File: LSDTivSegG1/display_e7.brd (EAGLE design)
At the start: 150 x 100 mm, 95 parts, among them IC1 MEGA8-P, IC2 MAX232, IC3 PCF8574P, IC4 PCF8574P, IC5 PCF8574P, IC6 PCF8574P

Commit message: exported the current version of the eagle 7 compatible file for display board
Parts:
- removed R4: 1k0, rcl:0207/10
- added C10, C11, C12, C13: 100nF, rcl:C025-025X050
- added JP2: (no value), pinhead:2X03
- R2: value 10k -> 5k
- R3: value 2k2 -> 15k
- U$2: value PCB -> DISPLAY_FRAME; device lsd2016:BOARD -> lsd2016:DISPLAY_FRAME
- moved LED19 255.4 mm to (127.0, 66.0), turned to 90 degrees
- moved R32 253.5 mm to (101.6, 38.1), turned to 270 degrees
- moved C7 246.0 mm to (121.9, 83.8), turned to 270 degrees
- moved IC6 245.8 mm to (137.2, 16.5), flipped to the bottom, turned to 180 degrees
- moved R31 242.0 mm to (99.1, 38.1), turned to 270 degrees
- moved LED18 234.9 mm to (119.4, 68.6), turned to 90 degrees
- moved R30 230.6 mm to (96.5, 38.1), turned to 270 degrees
- moved C5 229.5 mm to (121.9, 78.1), turned to 90 degrees
- moved IC2 229.5 mm to (108.6, 81.9)
- moved R5 227.3 mm to (82.5, 24.1)
- moved LED24 222.3 mm to (129.5, 27.9)
- moved U$1 221.2 mm to (113.0, 5.08), turned to 180 degrees
- moved JP1 220.3 mm to (73.7, 73.7), turned to 90 degrees
- moved R29 219.3 mm to (94.0, 38.1), turned to 270 degrees
- moved LED17 214.9 mm to (111.8, 68.6), turned to 90 degrees
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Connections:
- removed net VCC: IC2.16
- new net RS232RX_CON: JP2.3, X1.2
- new net RS232TX_CON: JP2.4, X1.3
- net +5V: now also C10.1, C11.1, C12.1, C13.1, IC2.16; no longer C6.-, R12.2, R13.2, R14.2, R15.2, R16.2, R17.2, R18.2, R19.2, R20.2, R21.2, R22.2, R23.2, R24.2, R25.2, R26.2, R27.2, R28.2, R29.2, R30.2, R31.2, R32.2, R33.2, R34.2, R35.2
- net GND: now also C10.2, C11.2, C12.2, C13.2, C6.-, R12.2, R13.2, R14.2, R15.2, R16.2, R17.2, R18.2, R19.2, R20.2, R21.2, R22.2, R23.2, R24.2, R25.2, R26.2, R27.2, R28.2, R29.2, R30.2, R31.2, R32.2, R33.2, R34.2, R35.2; no longer R4.2
- net N$9: no longer R4.1
- net RS232RX: now also JP2.1, JP2.6; no longer X1.4
- net RS232TX: now also JP2.2, JP2.5; no longer X1.3
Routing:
- net +5V: track 0.00 -> 159.8 mm
- net RW: track 0.00 -> 82.1 mm, vias 0 -> 1
- net RESET: track 0.00 -> 71.2 mm
- net RS232TX: track 0.00 -> 50.5 mm
- net N$34: track 0.00 -> 39.4 mm
- net N$22: track 0.00 -> 39.4 mm
- net RS232RX: track 0.00 -> 39.1 mm
- net N$35: track 0.00 -> 36.9 mm
- net N$23: track 0.00 -> 36.9 mm
- net N$21: track 0.00 -> 35.4 mm
- net N$33: track 0.00 -> 35.4 mm
- net N$32: track 0.00 -> 32.5 mm
- net N$20: track 0.00 -> 32.5 mm
- net N$19: track 0.00 -> 30.4 mm
- net N$31: track 0.00 -> 30.4 mm
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- added copper zone on layer 16, net GND
- removed copper zone on layer 1, net GND

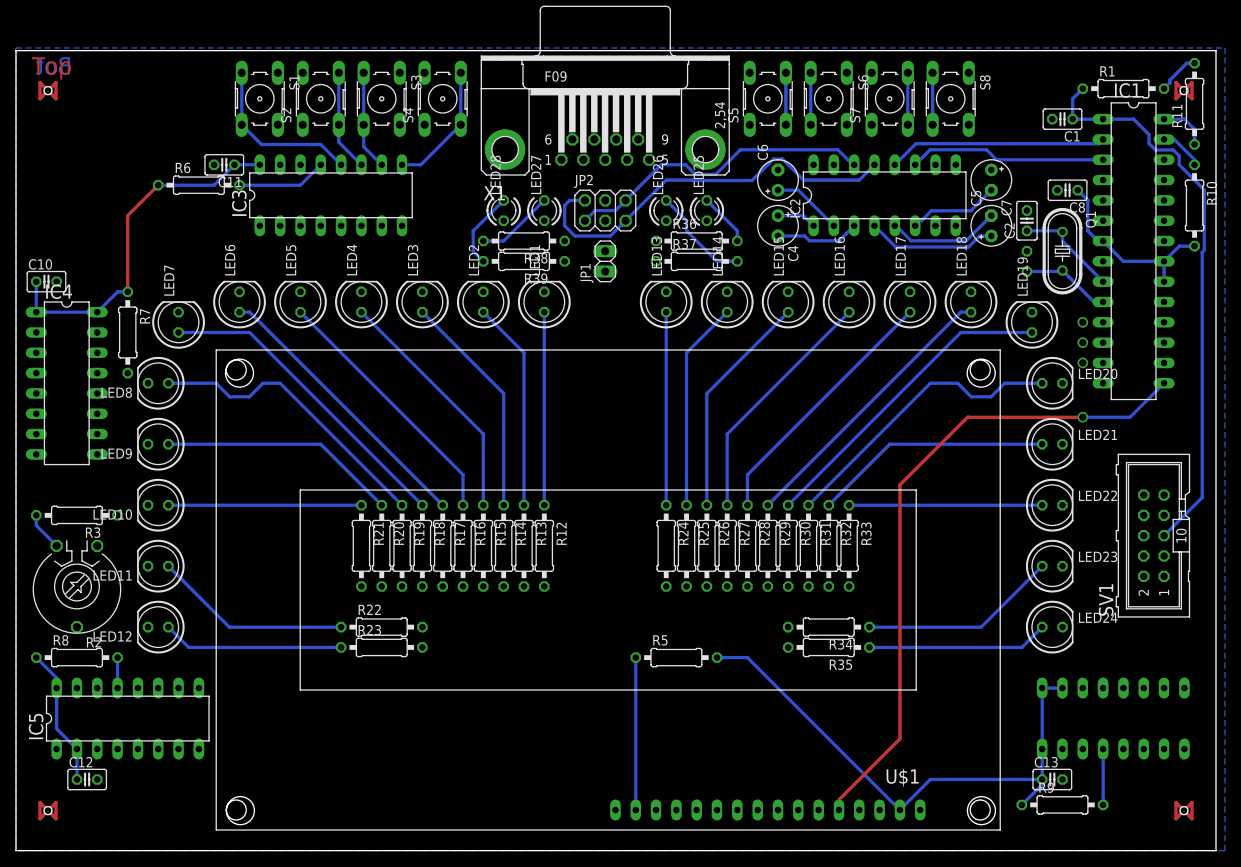
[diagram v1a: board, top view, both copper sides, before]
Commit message: updated eagle7 copatible exports of display and leistung boards
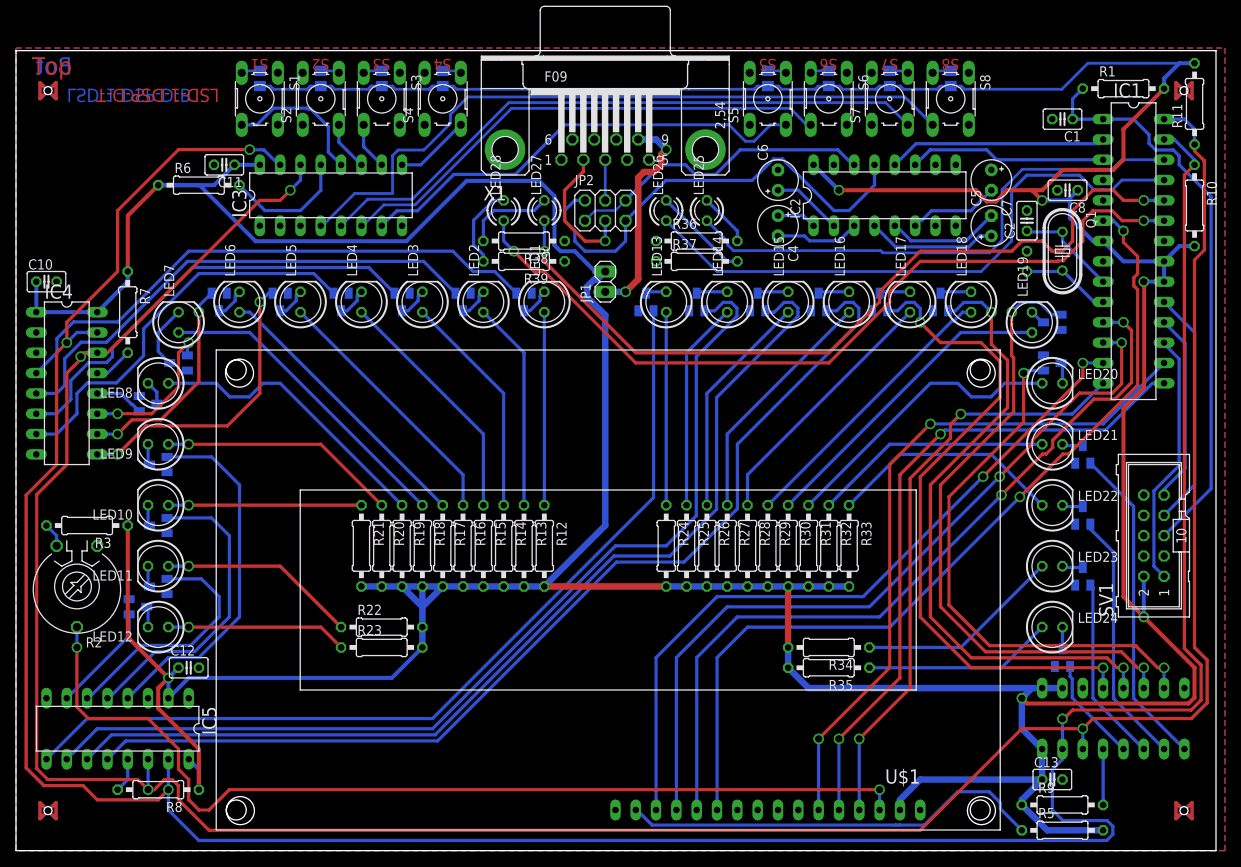
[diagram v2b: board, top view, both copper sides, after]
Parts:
- added R4, R40, R41, R42, R43, R44, R45, R46: 10k, rcl:R0805
- added T1, T10, T11, T12, T13, T14, T15, T16, T17, T18, T19, T2, T20, T21, T22, T23, T24, T3, T4, T5, T6, T7, T8, T9: BC847, transistor:SOT23
- moved R5 52.9 mm to (130.8, 2.54)
- moved R8 19.4 mm to (17.8, 7.62), turned to 180 degrees
- moved C12 18.9 mm to (21.6, 22.9)
- moved R7 2.54 mm to (14.0, 67.3)
- moved R34 2.54 mm to (101.6, 25.4)
- moved R35 2.54 mm to (101.6, 22.9)
- moved JP1 2.54 mm to (73.7, 71.1)
- moved IC5 1.80 mm to (12.7, 15.2), turned to 180 degrees
- moved R3 1.80 mm to (8.89, 40.6)
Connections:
- removed net SDL: IC3.14, IC4.14, IC5.14, IC6.14
- new net N$49: R4.1, S8.3
- new net N$50: R41.1, S6.3
- new net N$51: LED9.K, T9.3
- new net N$52: R45.1, S2.4
- new net N$53: LED1.K, T1.3
- new net N$54: LED2.K, T2.3
- new net N$55: LED3.K, T3.3
- new net N$56: LED4.K, T4.3
- new net N$57: LED5.K, T5.3
- new net N$58: LED6.K, T6.3
- new net N$59: LED17.K, T17.3
- new net N$60: LED10.K, T10.3
- new net N$61: LED11.K, T11.3
- new net N$62: LED12.K, T12.3
- new net N$63: LED13.K, T13.3
- new net N$64: LED14.K, T14.3
- new net N$65: LED7.K, T7.3
- new net N$66: LED8.K, T8.3
- new net N$67: LED15.K, T15.3
- new net N$68: LED16.K, T16.3
- new net N$69: LED18.K, T18.3
- new net N$70: LED19.K, T19.3
- new net N$71: LED20.K, T20.3
- new net N$72: LED21.K, T21.3
- new net N$73: LED22.K, T22.3
- new net N$74: LED23.K, T23.3
- new net N$75: LED24.K, T24.3
- new net N$76: R43.1, S4.4
- new net N$77: R44.1, S3.3
- new net N$78: R42.1, S5.4
- new net N$79: R46.1, S1.3
- new net N$80: R40.1, S7.4
- net +5V: now also R12.2, R13.2, R14.2, R15.2, R16.2, R17.2, R18.2, R19.2, R20.2, R21.2, R22.2, R23.2, R24.2, R25.2, R26.2, R27.2, R28.2, R29.2, R30.2, R31.2, R32.2, R33.2, R34.2, R35.2, R4.2, R40.2, R41.2, R42.2, R43.2, R44.2, R45.2, R46.2
- net BTN0: no longer S8.3
- net BTN1: no longer S7.4
- net BTN2: no longer S6.3
- net BTN3: no longer S5.4
- net BTN4: no longer S4.4
- net BTN5: no longer S3.3
- net BTN6: no longer S2.4
- net BTN7: no longer S1.3
- net GND: now also T1.2, T10.2, T11.2, T12.2, T13.2, T14.2, T15.2, T16.2, T17.2, T18.2, T19.2, T2.2, T20.2, T21.2, T22.2, T23.2, T24.2, T3.2, T4.2, T5.2, T6.2, T7.2, T8.2, T9.2; no longer R12.2, R13.2, R14.2, R15.2, R16.2, R17.2, R18.2, R19.2, R20.2, R21.2, R22.2, R23.2, R24.2, R25.2, R26.2, R27.2, R28.2, R29.2, R30.2, R31.2, R32.2, R33.2, R34.2, R35.2
- net LED0: now also T1.1; no longer LED1.K
- net LED1: now also T2.1; no longer LED2.K
- net LED10: now also T11.1; no longer LED11.K
- net LED11: now also T12.1; no longer LED12.K
- net LED12: now also T13.1; no longer LED13.K
- net LED13: now also T14.1; no longer LED14.K
- net LED14: now also T15.1; no longer LED15.K
- net LED15: now also T16.1; no longer LED16.K
- net LED16: now also T17.1; no longer LED17.K
- net LED17: now also T18.1; no longer LED18.K
- net LED18: now also T19.1; no longer LED19.K
- net LED19: now also T20.1; no longer LED20.K
- net LED2: now also T3.1; no longer LED3.K
- net LED20: now also T21.1; no longer LED21.K
- net LED21: now also T22.1; no longer LED22.K
- net LED22: now also T23.1; no longer LED23.K
- net LED23: now also T24.1; no longer LED24.K
- net LED3: now also T4.1; no longer LED4.K
- net LED4: now also T5.1; no longer LED5.K
- net LED5: now also T6.1; no longer LED6.K
- net LED6: now also T7.1; no longer LED7.K
- net LED7: now also T8.1; no longer LED8.K
- net LED8: now also T9.1; no longer LED9.K
- net LED9: now also T10.1; no longer LED10.K
- net SCL: now also IC3.14, IC4.14, IC5.14, IC6.14
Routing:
- net +5V: track 159.8 -> 707.3 mm, vias 0 -> 6
- net SDA: track 6.13 -> 362.7 mm, vias 0 -> 4
- net SCL: track 7.51 -> 336.8 mm, vias 0 -> 4
- net LED15: track 0.00 -> 127.9 mm
- net LED14: track 0.00 -> 125.9 mm
- net LED13: track 0.00 -> 124.2 mm
- net N$10: track 0.00 -> 122.2 mm, vias 0 -> 2
- net LED12: track 0.00 -> 112.8 mm
- net D4: track 0.00 -> 109.2 mm, vias 0 -> 2
- net N$40: track 0.00 -> 102.1 mm, vias 0 -> 2
- net N$41: track 0.00 -> 100.3 mm, vias 0 -> 2
- net D5: track 0.00 -> 98.7 mm, vias 0 -> 2
- net D6: track 0.00 -> 96.6 mm, vias 0 -> 2
- net D7: track 0.00 -> 91.2 mm, vias 0 -> 2
- net EN: track 0.00 -> 86.4 mm, vias 0 -> 2
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- added copper zone on layer 1, net GND
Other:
- board text added: "LSD-1-DSP-D-B"
- board text added: "LSD-1-DSP-D-BSTOP"
- board text added: "LSD-1-DSP-D-T"
- board text added: "LSD-1-DSP-D-TSTOP"
- board text added: "S1"
- board text added: "S2"
- board text added: "S3"
- board text added: "S4"
- board text added: "S5"
- board text added: "S6"
- board text added: "S7"
- board text added: "S8"

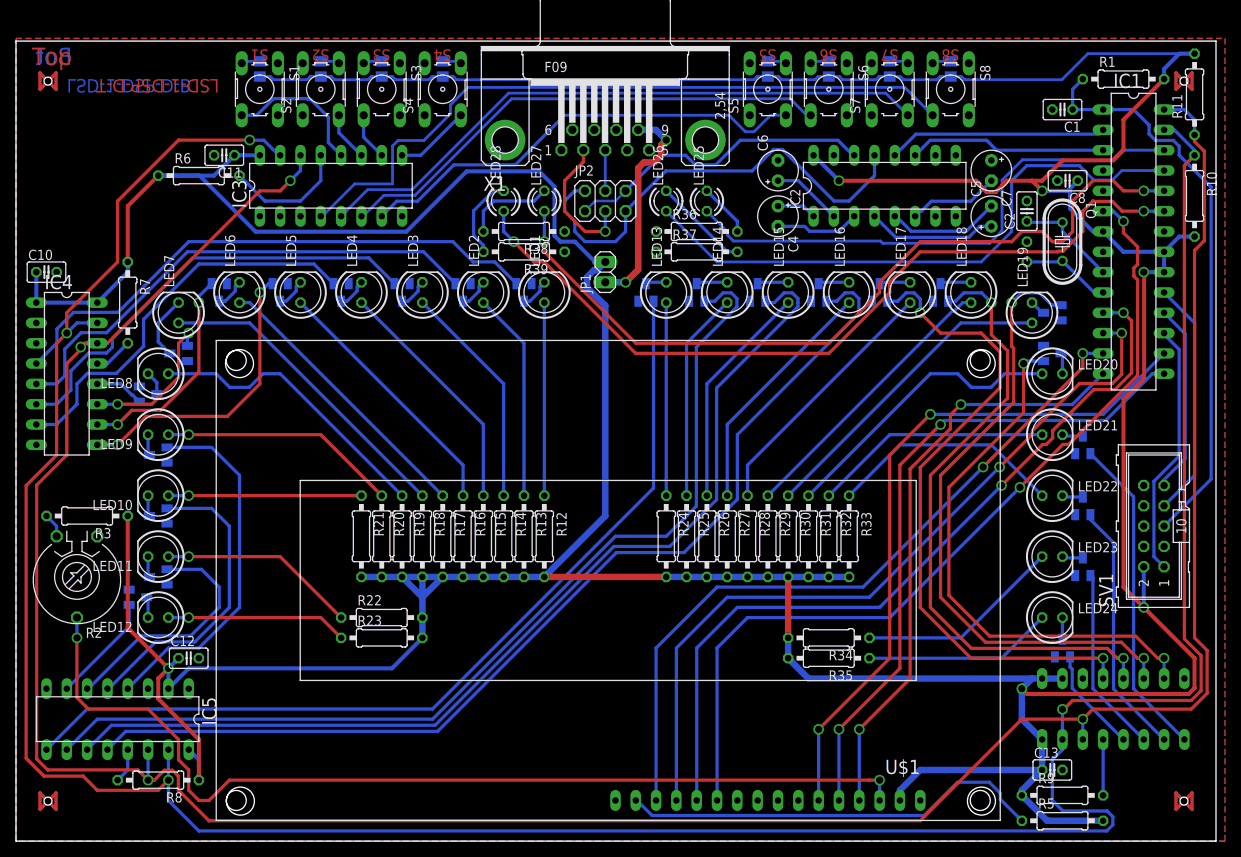
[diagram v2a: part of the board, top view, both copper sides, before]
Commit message: used isolation 20 for ground planes
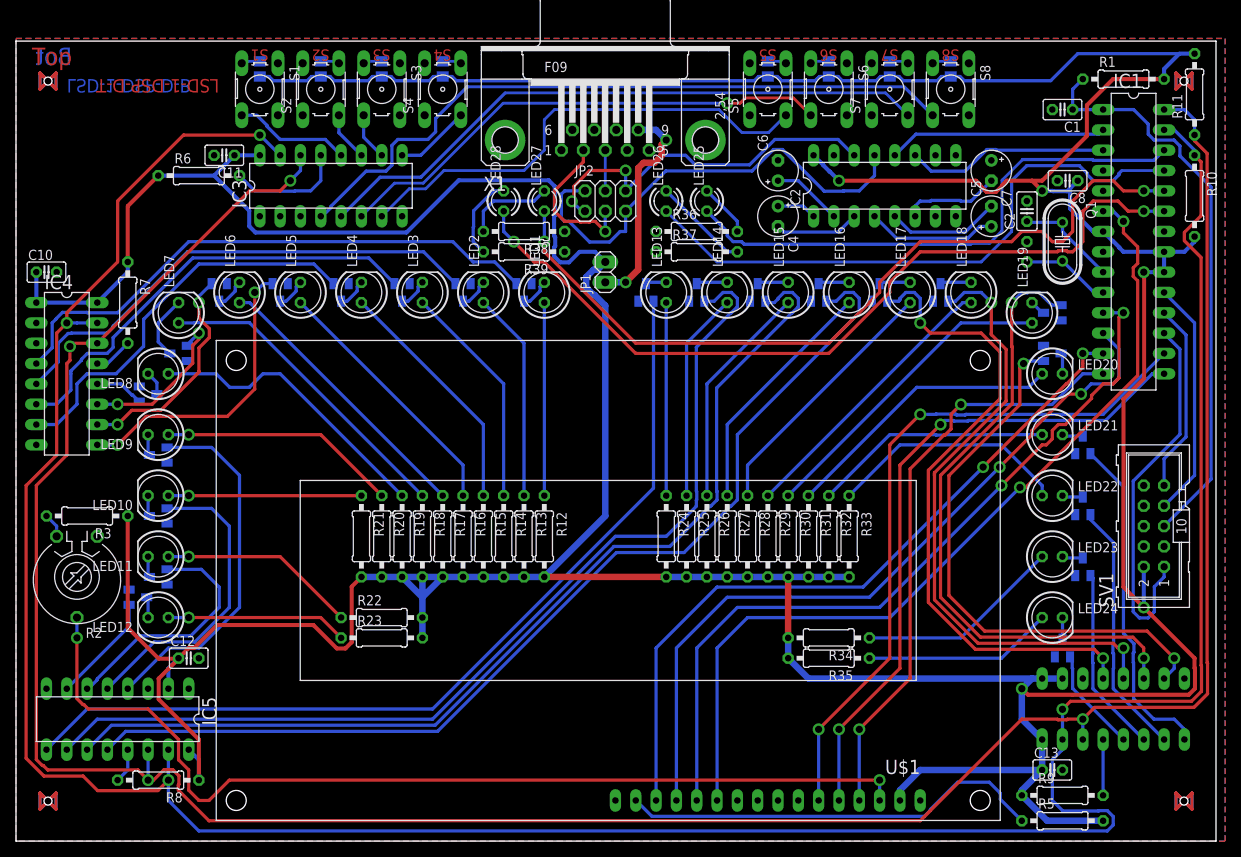
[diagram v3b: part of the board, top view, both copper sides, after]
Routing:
- net MOSI: track 31.8 -> 47.5 mm
- net RS232RX: track 39.1 -> 47.0 mm, vias 0 -> 2
- net BTN7: track 18.1 -> 14.6 mm
- net BTN3: track 57.5 -> 60.4 mm
- net SCL: track 336.8 -> 334.8 mm
- net RS232RX_CON: track 17.3 -> 19.1 mm
- net LED19: track 68.2 -> 70.0 mm
- net LED20: track 40.6 -> 42.2 mm
- net D6: track 96.6 -> 95.1 mm
- net N$35: track 36.9 -> 35.5 mm
- net LED5: track 27.1 -> 28.3 mm
- net D5: track 98.7 -> 97.6 mm
- net LED6: track 19.3 -> 20.4 mm
- net N$12: track 15.7 -> 14.7 mm
- net SDA: track 362.7 -> 363.7 mm
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
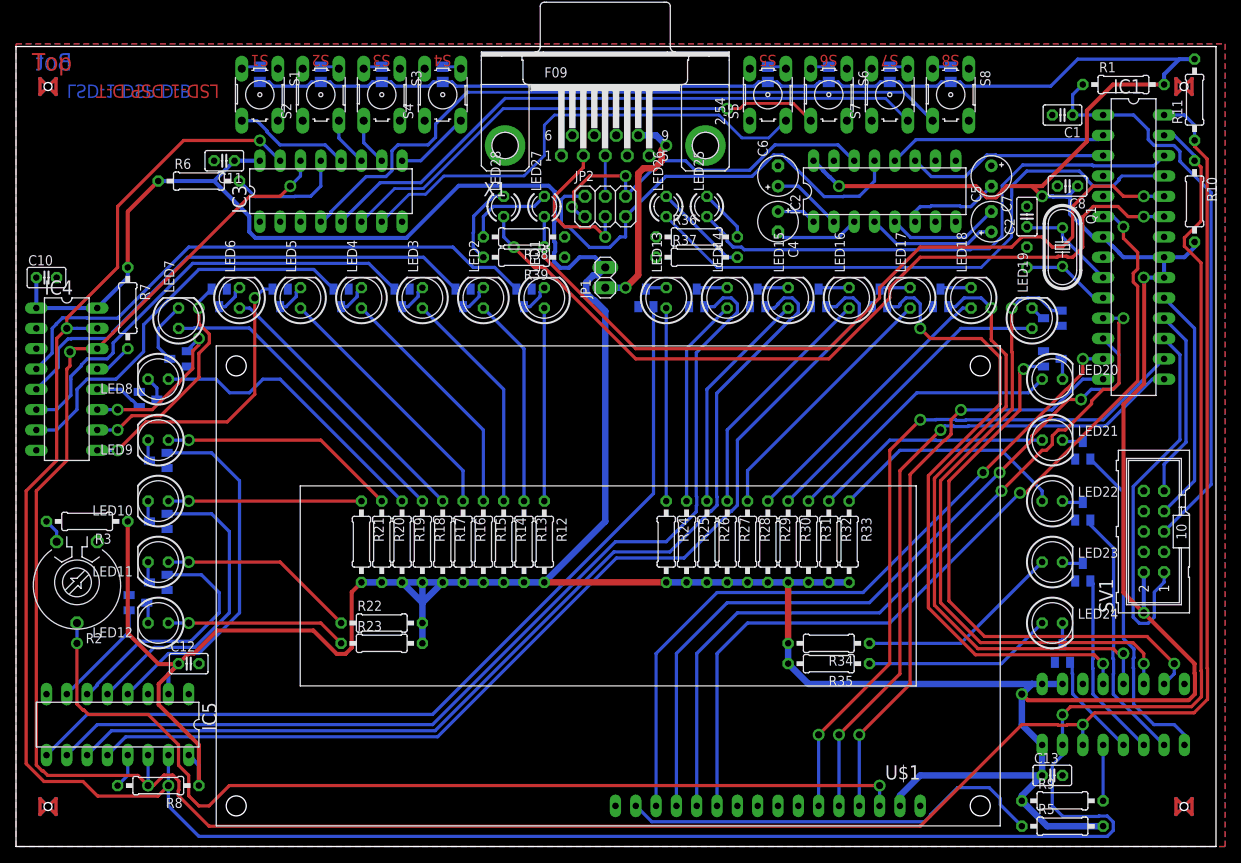
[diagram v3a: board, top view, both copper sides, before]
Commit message: updated e7 compatible version of display
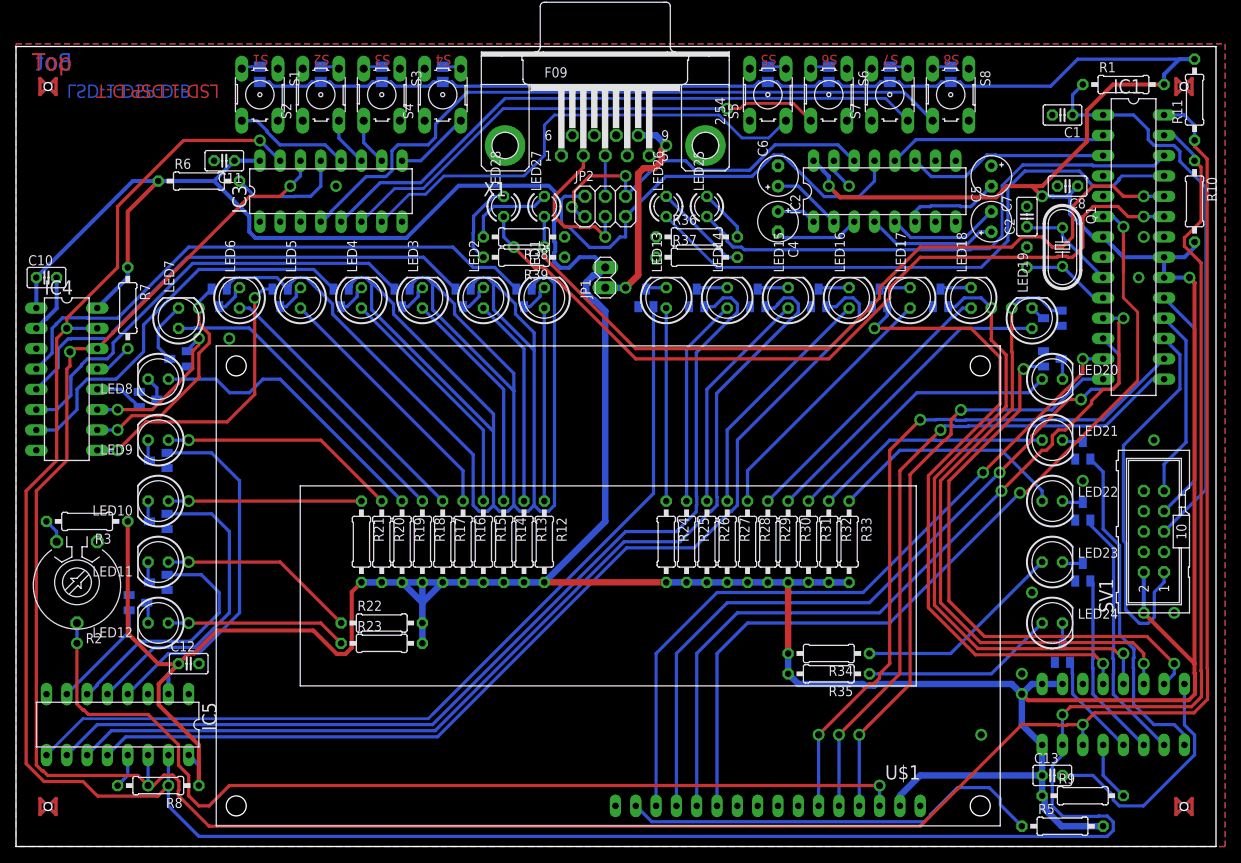
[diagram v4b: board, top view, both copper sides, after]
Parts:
- moved R9 2.62 mm to (133.3, 6.35)
- moved R34 1.27 mm to (101.6, 24.1)
- moved R35 1.27 mm to (101.6, 21.6)
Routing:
- net GND: track 0.00 -> 299.5 mm, vias 0 -> 11
- net +5V: track 706.5 -> 720.4 mm
- net LED16: track 81.8 -> 82.8 mm
- net MOSI: track 47.5 -> 48.5 mm
- net N$38: track 25.8 -> 26.3 mm
- net N$39: track 23.7 -> 24.2 mm
- net RESET: track 71.9 -> 71.4 mm
